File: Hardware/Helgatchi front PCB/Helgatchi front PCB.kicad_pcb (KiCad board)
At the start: 2 copper layers, 50 x 80 mm, 34 parts, among them J1 BATTERY, J2 SCREEN, M1 MOTOR, Q1 NMOS, SW1 LEFT BUTTON, SW2 CENTER BUTTON, SW3 RIGHT BUTTON, U1 XIAO ESP32-S3

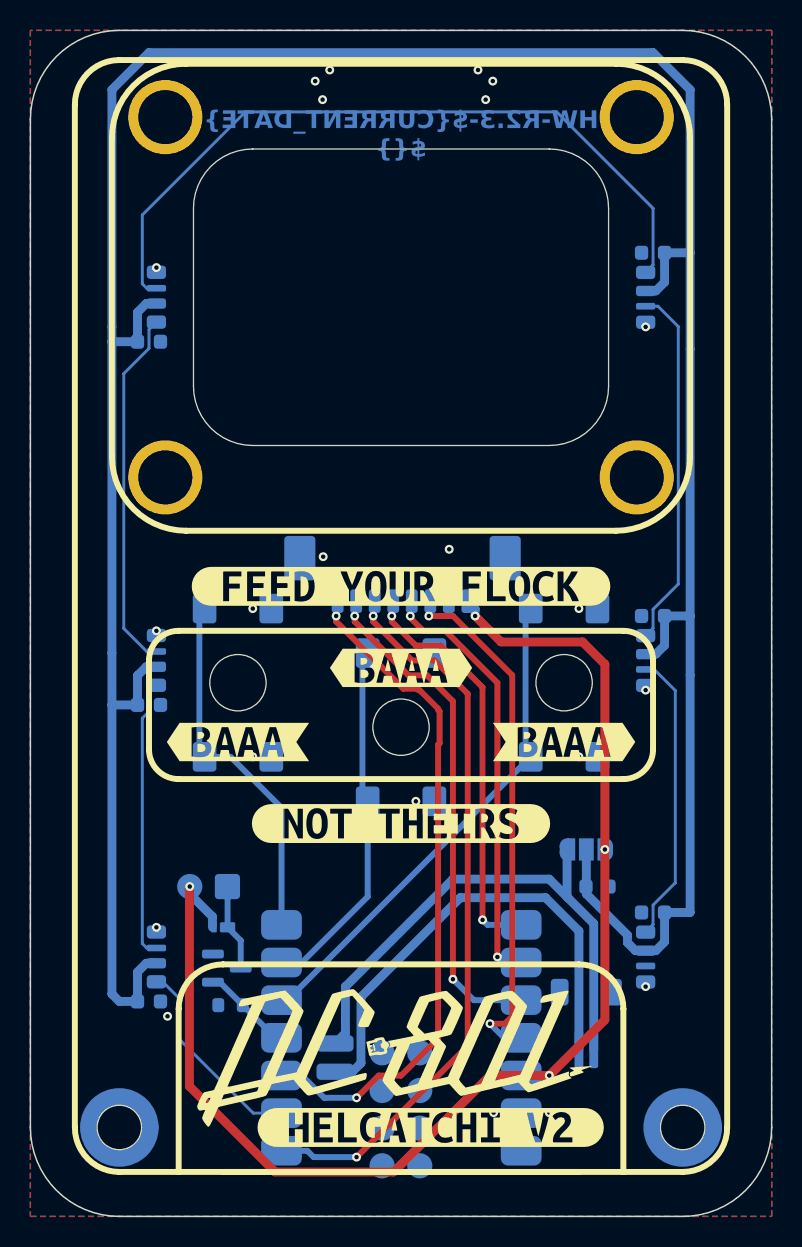
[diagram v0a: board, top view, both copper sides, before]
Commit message: Swap <baaa> for (baaa)
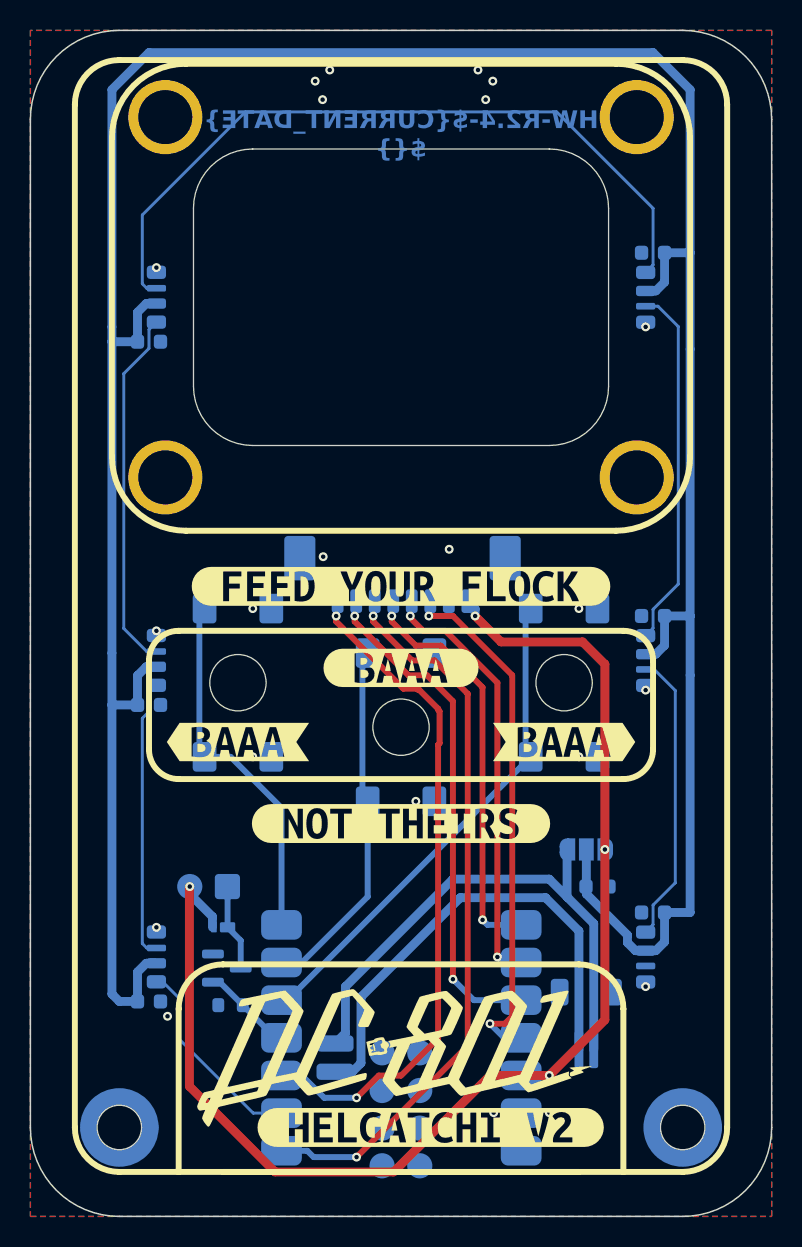
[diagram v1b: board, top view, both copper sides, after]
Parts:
- removed kibuzzard-6976EA63: G***, kibuzzard-6976EA63
- added kibuzzard-69862DFC: G***, kibuzzard-69862DFC, F.Cu at (164.0, 101.5)

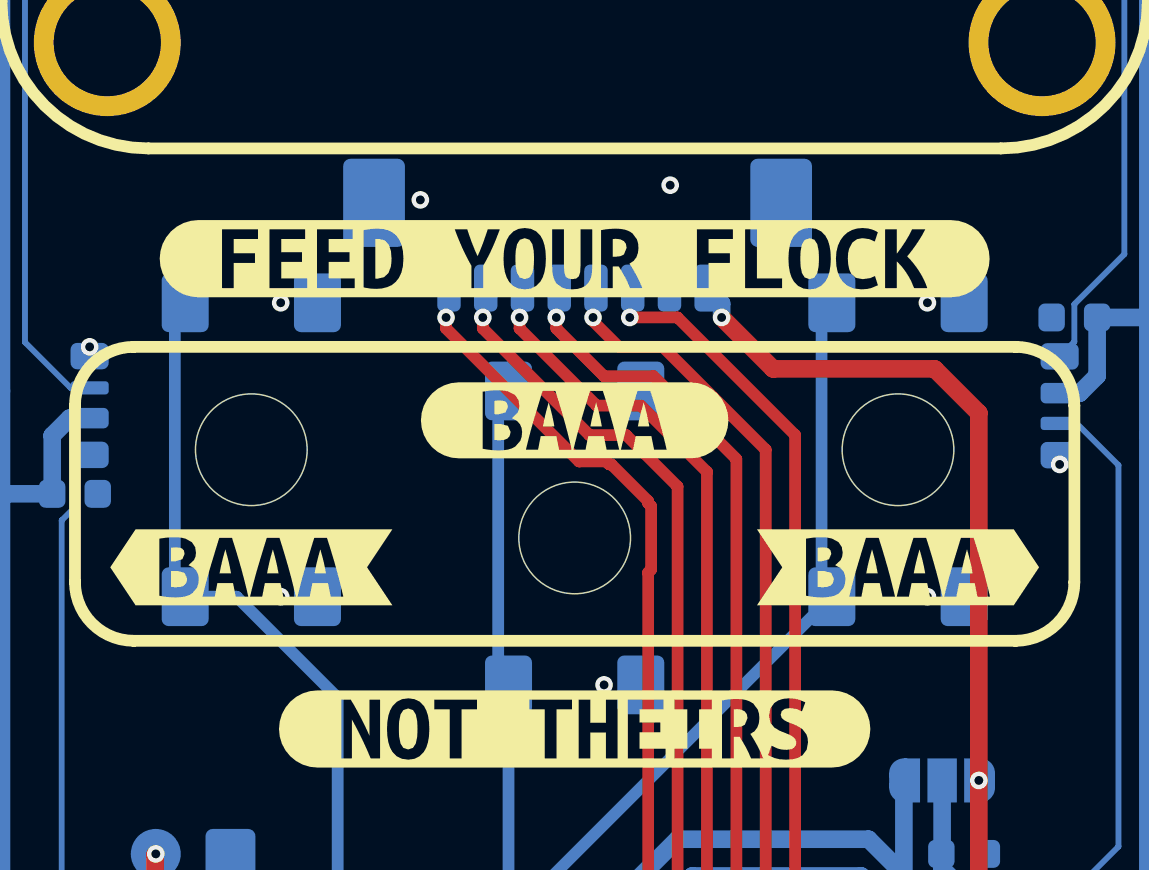
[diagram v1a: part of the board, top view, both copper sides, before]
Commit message: Add via in pads for buttons
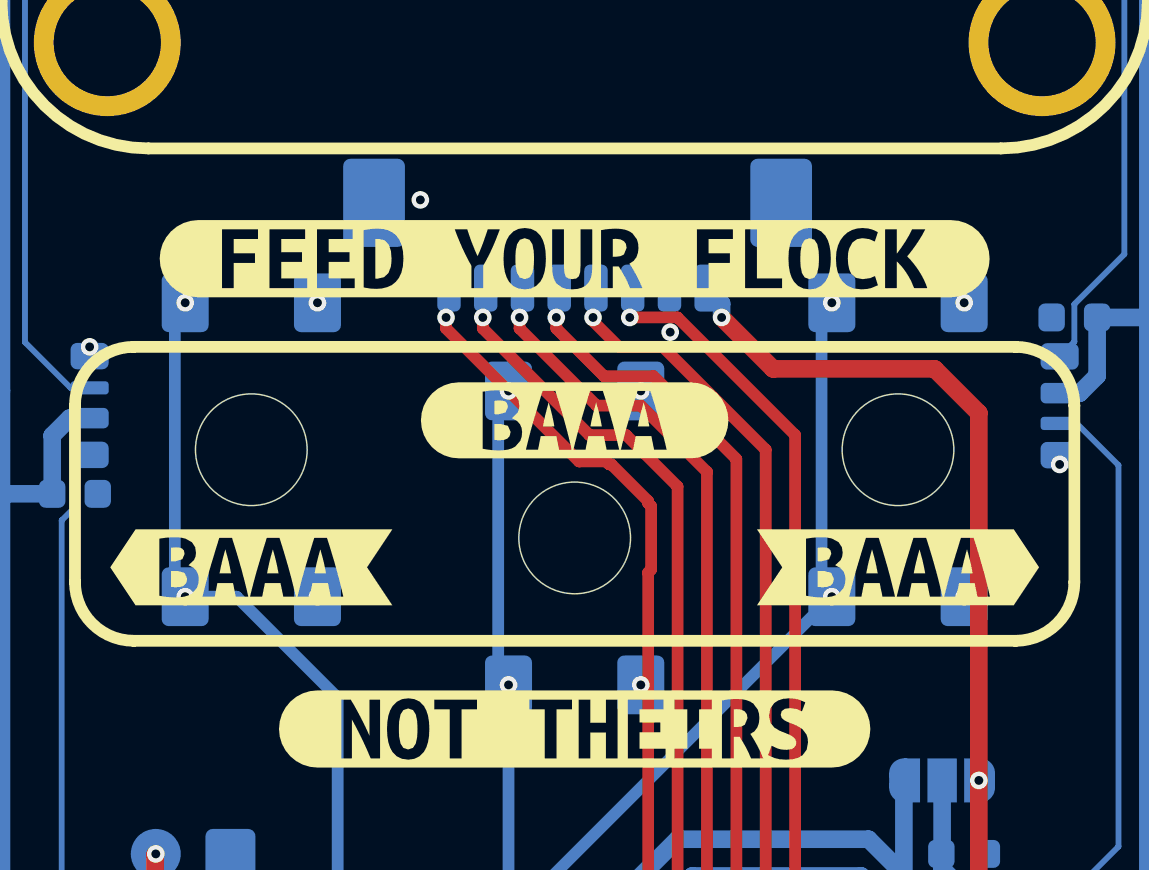
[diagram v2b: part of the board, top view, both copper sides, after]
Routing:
- net GND: vias 16 -> 17
- net BUTTON_RIGHT: vias 0 -> 2
- net BUTTON_LEFT: vias 0 -> 2
- net BUTTON_CENTER: vias 0 -> 2
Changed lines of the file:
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@@
 	)
 	(via
-		(at 154 97.5)
-		(size 0.6)
-		(drill 0.3)
-		(layers "F.Cu" "B.Cu")
-		(free yes)
+		(at 166.25 100.5)
+		(size 0.6)
+		(drill 0.3)
+		(layers "F.Cu" "B.Cu")
 		(net 15)
 	)
@@
 	)
 	(via
-		(at 154 107.5)
-		(size 0.6)
-		(drill 0.3)
-		(layers "F.Cu" "B.Cu")
-		(free yes)
-		(net 15)
-	)
-	(via
-		(at 167.25 93.5)
-		(size 0.6)
-		(drill 0.3)
-		(layers "F.Cu" "B.Cu")
-		(free yes)
+		(at 166.25 110.5)
+		(size 0.6)
+		(drill 0.3)
+		(layers "F.Cu" "B.Cu")
+		(net 15)
+	)
+	(via
+		(at 155.25 107.5)
+		(size 0.6)
+		(drill 0.3)
+		(layers "F.Cu" "B.Cu")
+		(net 15)
+	)
+	(via
+		(at 177.25 107.5)
+		(size 0.6)
+		(drill 0.3)
+		(layers "F.Cu" "B.Cu")
 		(net 15)
 	)
@@
 	)
 	(via
+		(at 155.25 97.5)
+		(size 0.6)
+		(drill 0.3)
+		(layers "F.Cu" "B.Cu")
+		(net 15)
+	)
+	(via
 		(at 147.5 99)
 		(size 0.6)
@@
 	)
 	(via
+		(at 177.25 97.5)
+		(size 0.6)
+		(drill 0.3)
+		(layers "F.Cu" "B.Cu")
+		(net 15)
+	)
+	(via
 		(at 180.5 78.5)
 		(size 0.6)
@@
 	)
 	(via
+		(at 167.25 98.5)
+		(size 0.6)
+		(drill 0.3)
+		(layers "F.Cu" "B.Cu")
+		(free yes)
+		(net 15)
+	)
+	(via
 		(at 147.5 74.5)
 		(size 0.6)
@@
 	)
 	(via
-		(at 176 97.5)
-		(size 0.6)
-		(drill 0.3)
-		(layers "F.Cu" "B.Cu")
-		(free yes)
-		(net 15)
-	)
-	(via
 		(at 158.75 94)
 		(size 0.6)
@@
 	(via
 		(at 148.25 125)
-		(size 0.6)
-		(drill 0.3)
-		(layers "F.Cu" "B.Cu")
-		(free yes)
-		(net 15)
-	)
-	(via
-		(at 176 107.5)
-		(size 0.6)
-		(drill 0.3)
-		(layers "F.Cu" "B.Cu")
-		(free yes)
-		(net 15)
-	)
-	(via
-		(at 165 110.5)
 		(size 0.6)
 		(drill 0.3)
@@
 		(net 25)
 	)
+	(via
+		(at 150.75 97.5)
+		(size 0.6)
+		(drill 0.3)
+		(layers "F.Cu" "B.Cu")
+		(net 26)
+	)
+	(via
+		(at 150.75 107.5)
+		(size 0.6)
+		(drill 0.3)
+		(layers "F.Cu" "B.Cu")
+		(net 26)
+	)
 	(segment
 		(start 155.938636 118.833)
@@
 		(net 26)
 	)
+	(via
+		(at 161.75 100.5)
+		(size 0.6)
+		(drill 0.3)
+		(layers "F.Cu" "B.Cu")
+		(net 27)
+	)
+	(via
+		(at 161.75 110.5)
+		(size 0.6)
+		(drill 0.3)
+		(layers "F.Cu" "B.Cu")
+		(net 27)
+	)
 	(segment
 		(start 155.938636 121.373)
@@
 		(net 27)
 	)
-	(segment
+	(via
+		(at 172.75 97.5)
+		(size 0.6)
+		(drill 0.3)
+		(layers "F.Cu" "B.Cu")
+		(net 28)
+	)
+	(via
+		(at 172.75 107.5)
+		(size 0.6)
+		(drill 0.3)
+		(layers "F.Cu" "B.Cu")
+		(net 28)
+	)
+	(segment

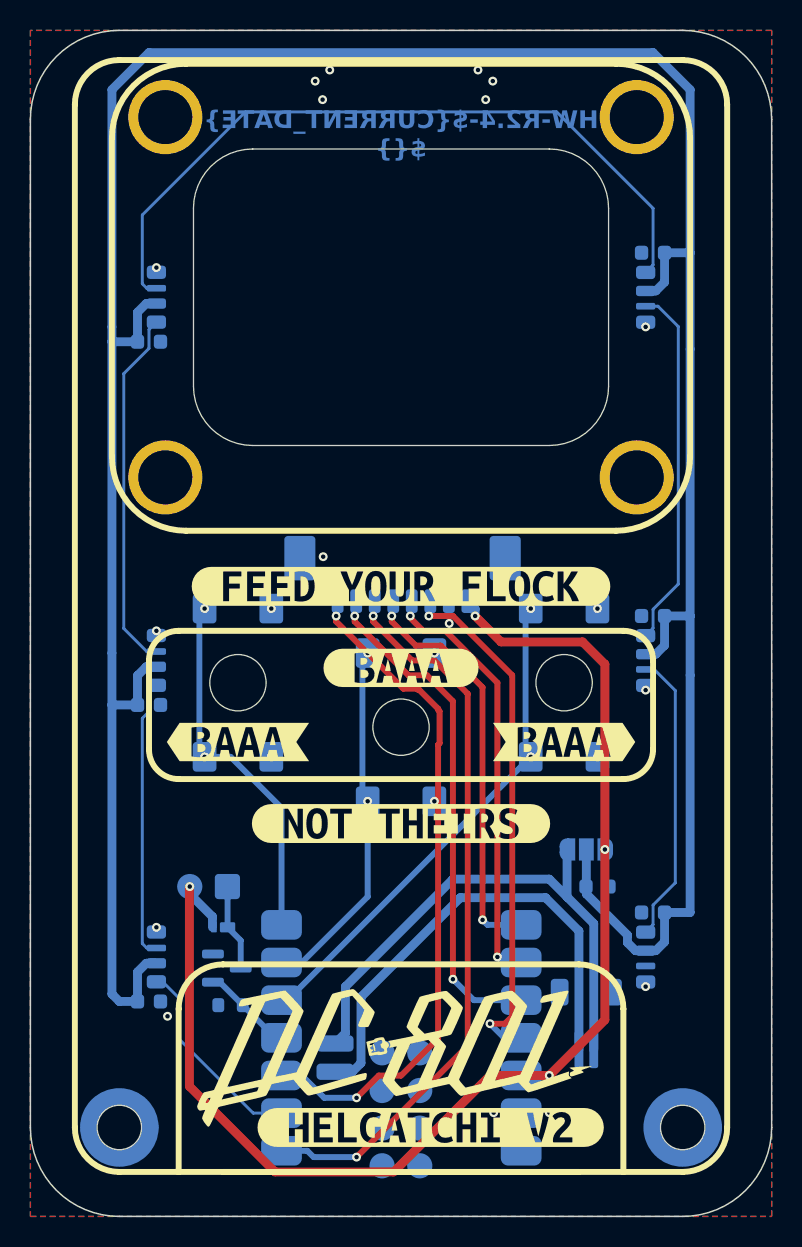
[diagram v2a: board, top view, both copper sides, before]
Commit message: Helgatchi front PCB: update to R2.5
Bump PCB revision to R2.5 and apply small layout/text tweaks: adjust gr_text position, update render_cache label/date, add font thickness to silkscreen effects, and shift numerous silkscreen/graphics coordinates. Also update corresponding schematic and netlist, and add production archives (Helgatchi_Front_R2.4.zip and a backups zip).
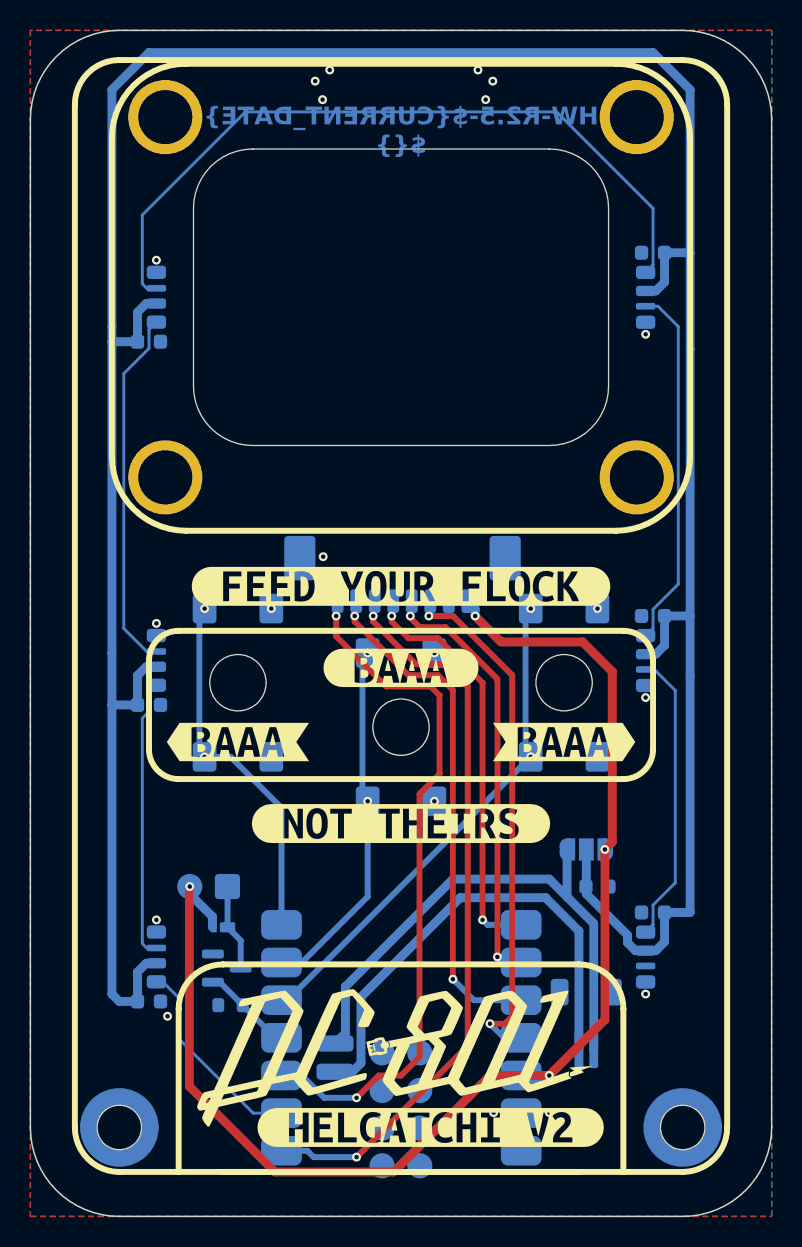
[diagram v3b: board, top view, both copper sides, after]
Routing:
- net SPI_BL: track 46.0 -> 47.1 mm
- net GND: vias 17 -> 16

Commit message: Bump Helgatchi front PCB to R2.6
Update KiCad board revision to R2.6 and apply minor footprint/silkscreen geometry adjustments (including PROTOTYPE silkscreen and render_cache updates dated 2026-02-11). Add production archives and backups for the front PCB (R2.5 and R2.6 .zip exports). Update netlist.ipc to reflect the PCB changes.
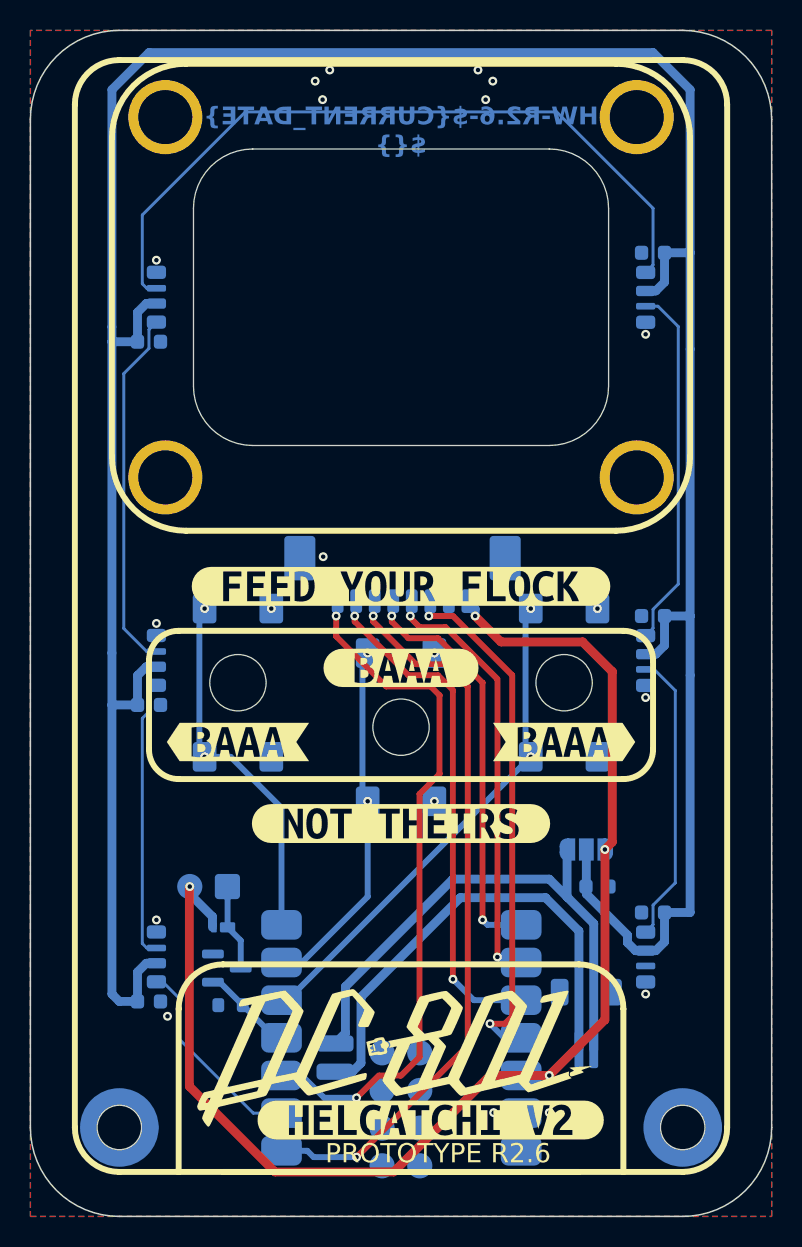
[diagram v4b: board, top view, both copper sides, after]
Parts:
- moved kibuzzard-6976EDA9 0.50 mm to (166.0, 132.0)
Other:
- board text added: "PROTOTYPE ${REVISION}"
